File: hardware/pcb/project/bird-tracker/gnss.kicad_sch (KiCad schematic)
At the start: 6 parts, among them U2 SAM-M10Q-00B

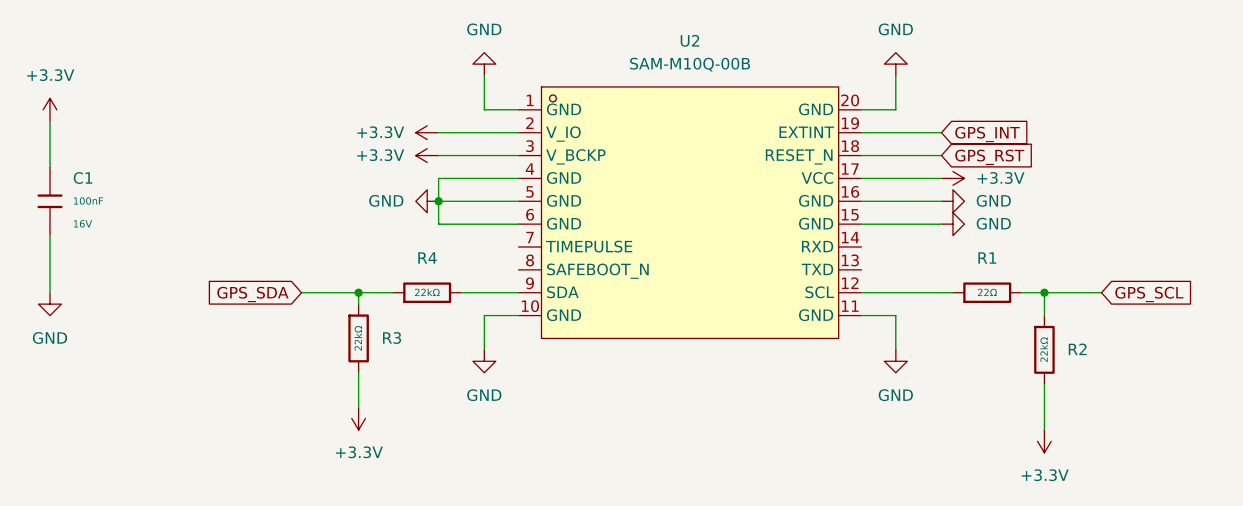
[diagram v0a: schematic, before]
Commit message: GNSS sheet complete
Revision v0.1
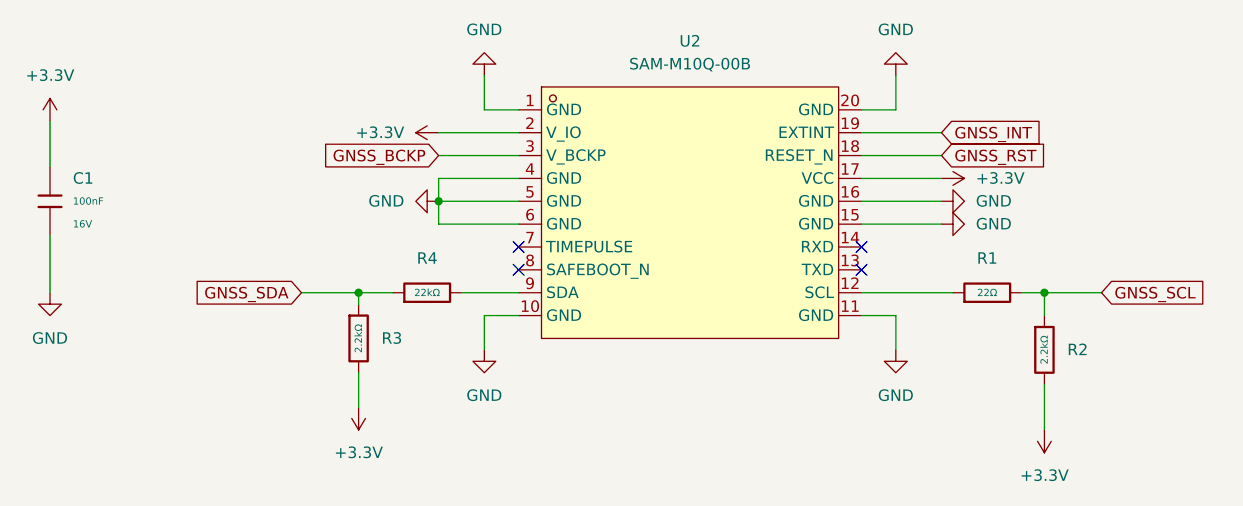
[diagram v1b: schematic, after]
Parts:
- removed R2, R3: 22kΩ, PCM_JLCPCB:R_0402, symbol PCM_JLCPCB-Resistors:0402,22kΩ
- added R2, R3: 2.2kΩ, PCM_JLCPCB:R_0402, symbol PCM_JLCPCB-Resistors:0402,2.2kΩ
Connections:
- net +3.3V: now also R2.2, R3.2; no longer U2.3 (V_BCKP)
- net GPS_INT renamed GNSS_INT
- net GPS_RST renamed GNSS_RST
- net GPS_SCL renamed GNSS_SCL
- net GNSS_SCL: now also R2.1
- net GPS_SDA renamed GNSS_SDA
- net GNSS_SDA: now also R3.1
- new net GNSS_BCKP: U2.3 (V_BCKP)
- no-connect marks 0 -> 4
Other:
- title: (none) -> Bird Tracker - GNSS
